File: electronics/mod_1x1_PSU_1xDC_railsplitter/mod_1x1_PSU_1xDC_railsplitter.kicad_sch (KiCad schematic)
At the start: 53 parts, among them J1 module_2x15_left_input, J2 module_2x15_right_input, J3 Jack-DC, J5 Conn_01x02, U1 LD1117, U2 LM317, U3 LM337, U4 LD1117, U5 TLV431

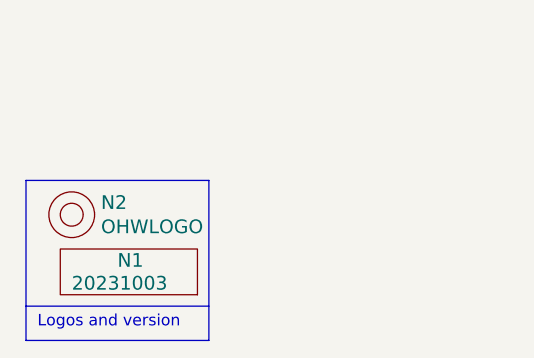
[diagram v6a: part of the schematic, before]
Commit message: fixing DRC errors
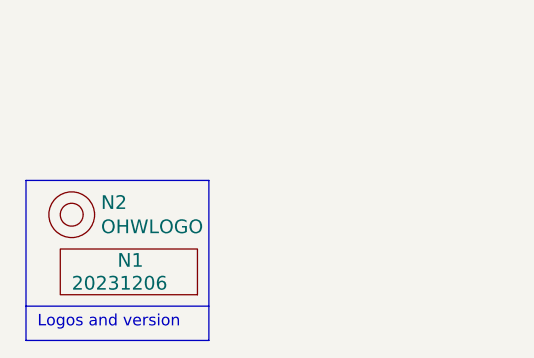
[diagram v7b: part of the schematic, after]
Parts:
- N1: value 20231003 -> 20231206
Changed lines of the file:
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@@
       (effects (font (size 1.524 1.524)) (justify left))
     )
-    (property "Value" "20231003" (at 19.05 189.23 0)
+    (property "Value" "20231206" (at 19.05 189.23 0)
       (effects (font (size 1.524 1.524)) (justify left))
     )

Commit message: fixed last DRC errors
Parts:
- N1: value 20231206 -> 20231208
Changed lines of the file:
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@@
       (effects (font (size 1.524 1.524)) (justify left))
     )
-    (property "Value" "20231206" (at 19.05 189.23 0)
+    (property "Value" "20231208" (at 19.05 189.23 0)
       (effects (font (size 1.524 1.524)) (justify left))
     )
